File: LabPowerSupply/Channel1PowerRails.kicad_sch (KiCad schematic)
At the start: 8 parts

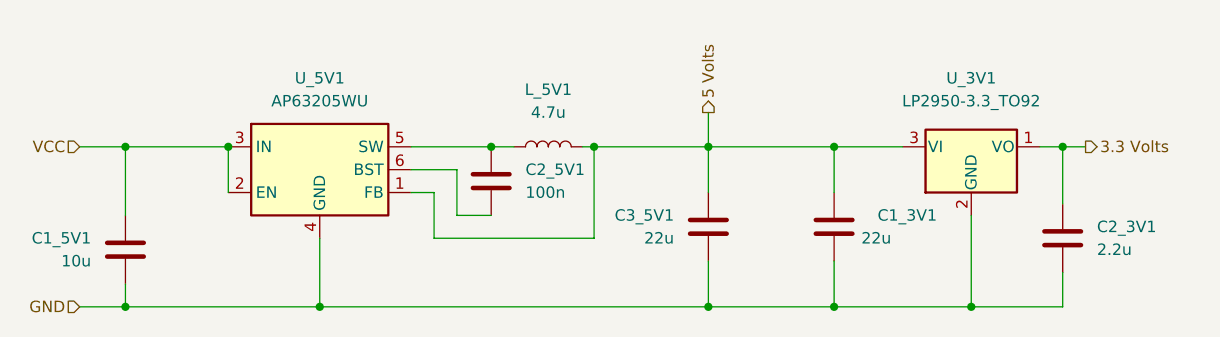
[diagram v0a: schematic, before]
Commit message: Fixed 3.3v footprint
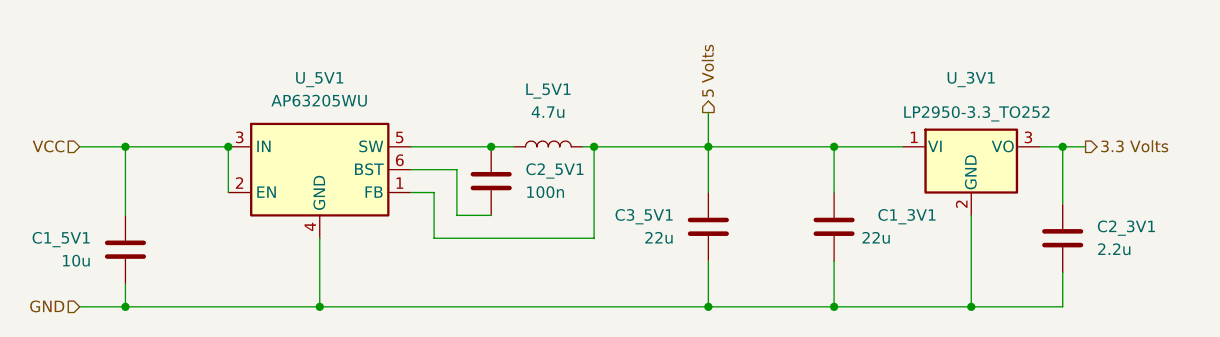
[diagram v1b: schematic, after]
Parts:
- U_3V1: value LP2950-3.3_TO92 -> LP2950-3.3_TO252; footprint Package_TO_SOT_SMD:TO-252-3_TabPin4 -> Package_TO_SOT_SMD:TO-252-2; symbol Regulator_Linear:LP2950-3.3_TO92 -> Regulator_Linear:LP2950-3.3_TO252
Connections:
- net 3.3 Volts: now also U_3V1.3 (VO); no longer U_3V1.1 (VO)
- net 5 Volts: now also U_3V1.1 (VI); no longer U_3V1.3 (VI)
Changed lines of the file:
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@@
     (pin "2")
   )
-  (symbol (lib_id "Regulator_Linear:LP2950-3.3_TO92") (at 196.85 88.9 0) (unit 1)
-    (in_bom yes) (on_board yes) (fields_autoplaced)
+  (symbol (lib_id "Regulator_Linear:LP2950-3.3_TO252") (at 196.85 88.9 0) (unit 1)
+    (in_bom yes) (on_board yes)
     (property "Reference" "U_3V1" (id 0) (at 196.85 81.28 0))
-    (property "Value" "LP2950-3.3_TO92" (id 1) (at 196.85 83.82 0))
-    (property "Footprint" "Package_TO_SOT_SMD:TO-252-3_TabPin4" (id 2) (at 196.85 83.185 0)
+    (property "Value" "LP2950-3.3_TO252" (id 1) (at 189.23 85.09 0)
+      (effects (font (size 1.27 1.27)) (justify left))
+    )
+    (property "Footprint" "Package_TO_SOT_SMD:TO-252-2" (id 2) (at 196.85 83.185 0)
       (effects (font (size 1.27 1.27) italic) hide)
     )

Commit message: Updated Part List
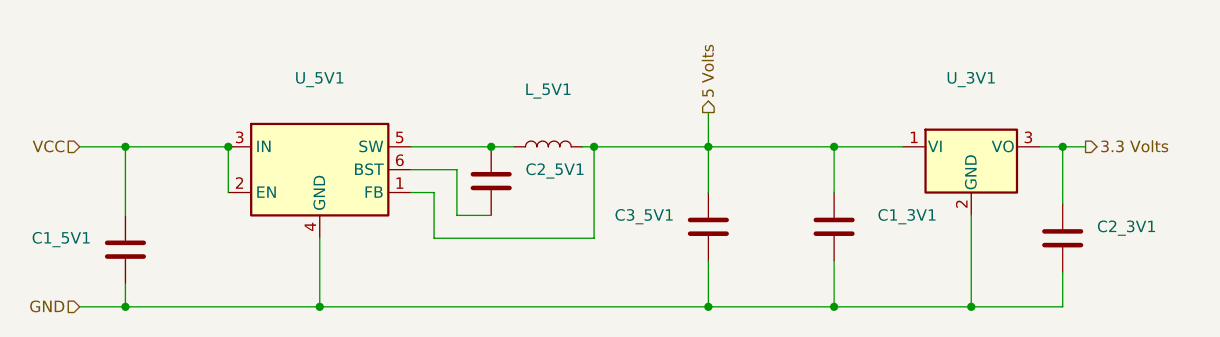
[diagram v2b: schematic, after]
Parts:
- C1_3V1, C3_5V1: value 22u -> (none); footprint Capacitor_SMD:C_1210_3225Metric -> (none)
- C1_5V1: value 10u -> (none); footprint Capacitor_SMD:C_1206_3216Metric -> (none)
- C2_3V1: value 2.2u -> (none); footprint Capacitor_SMD:C_0805_2012Metric -> (none)
- C2_5V1: value 100n -> (none); footprint Capacitor_SMD:C_0603_1608Metric -> (none)
- L_5V1: value 4.7u -> (none); footprint Inductor_SMD:L_Sumida_CDMC6D28_7.25x6.5mm -> (none)
- U_3V1: value LP2950-3.3_TO252 -> (none); footprint Package_TO_SOT_SMD:TO-252-2 -> (none)
- U_5V1: value AP63205WU -> (none); footprint Package_TO_SOT_SMD:TSOT-23-6 -> (none)
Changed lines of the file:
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@@
       (effects (font (size 1.27 1.27)) (justify right))
     )
-    (property "Value" "22u" (id 1) (at 187.96 99.06 0)
+    (property "Value" "" (id 1) (at 187.96 99.06 0)
       (effects (font (size 1.27 1.27)) (justify right))
     )
-    (property "Footprint" "Capacitor_SMD:C_1210_3225Metric" (id 2) (at 182.5752 93.98 0)
+    (property "Footprint" "" (id 2) (at 182.5752 93.98 0)
       (effects (font (size 1.27 1.27)) hide)
     )
@@
       (effects (font (size 1.27 1.27)) (justify left))
     )
-    (property "Value" "2.2u" (id 1) (at 210.82 100.3299 0)
+    (property "Value" "" (id 1) (at 210.82 100.3299 0)
       (effects (font (size 1.27 1.27)) (justify left))
     )
-    (property "Footprint" "Capacitor_SMD:C_0805_2012Metric" (id 2) (at 207.9752 102.87 0)
+    (property "Footprint" "" (id 2) (at 207.9752 102.87 0)
       (effects (font (size 1.27 1.27)) hide)
     )
@@
     (in_bom yes) (on_board yes) (fields_autoplaced)
     (property "Reference" "L_5V1" (id 0) (at 149.86 82.55 90))
-    (property "Value" "4.7u" (id 1) (at 149.86 85.09 90))
-    (property "Footprint" "Inductor_SMD:L_Sumida_CDMC6D28_7.25x6.5mm" (id 2) (at 149.86 88.9 0)
+    (property "Value" "" (id 1) (at 149.86 85.09 90))
+    (property "Footprint" "" (id 2) (at 149.86 88.9 0)
       (effects (font (size 1.27 1.27)) hide)
     )
@@
     (in_bom yes) (on_board yes)
     (property "Reference" "U_3V1" (id 0) (at 196.85 81.28 0))
-    (property "Value" "LP2950-3.3_TO252" (id 1) (at 189.23 85.09 0)
+    (property "Value" "" (id 1) (at 189.23 85.09 0)
       (effects (font (size 1.27 1.27)) (justify left))
     )
-    (property "Footprint" "Package_TO_SOT_SMD:TO-252-2" (id 2) (at 196.85 83.185 0)
+    (property "Footprint" "" (id 2) (at 196.85 83.185 0)
       (effects (font (size 1.27 1.27) italic) hide)
     )
@@
       (effects (font (size 1.27 1.27)) (justify right))
     )
-    (property "Value" "10u" (id 1) (at 99.06 101.5999 0)
+    (property "Value" "" (id 1) (at 99.06 101.5999 0)
       (effects (font (size 1.27 1.27)) (justify right))
     )
-    (property "Footprint" "Capacitor_SMD:C_1206_3216Metric" (id 2) (at 103.8352 96.52 0)
+    (property "Footprint" "" (id 2) (at 103.8352 96.52 0)
       (effects (font (size 1.27 1.27)) hide)
     )
@@
       (effects (font (size 1.27 1.27)) (justify right))
     )
-    (property "Value" "22u" (id 1) (at 163.83 99.0599 0)
+    (property "Value" "" (id 1) (at 163.83 99.0599 0)
       (effects (font (size 1.27 1.27)) (justify right))
     )
-    (property "Footprint" "Capacitor_SMD:C_1210_3225Metric" (id 2) (at 168.6052 93.98 0)
+    (property "Footprint" "" (id 2) (at 168.6052 93.98 0)
       (effects (font (size 1.27 1.27)) hide)
     )
@@
       (effects (font (size 1.27 1.27)) (justify left))
     )
-    (property "Value" "100n" (id 1) (at 147.32 93.9799 0)
+    (property "Value" "" (id 1) (at 147.32 93.9799 0)
       (effects (font (size 1.27 1.27)) (justify left))
     )
-    (property "Footprint" "Capacitor_SMD:C_0603_1608Metric" (id 2) (at 144.4752 96.52 0)
+    (property "Footprint" "" (id 2) (at 144.4752 96.52 0)
       (effects (font (size 1.27 1.27)) hide)
     )
@@
     (in_bom yes) (on_board yes) (fields_autoplaced)
     (property "Reference" "U_5V1" (id 0) (at 124.46 81.28 0))
-    (property "Value" "AP63205WU" (id 1) (at 124.46 83.82 0))
-    (property "Footprint" "Package_TO_SOT_SMD:TSOT-23-6" (id 2) (at 124.46 114.3 0)
+    (property "Value" "" (id 1) (at 124.46 83.82 0))
+    (property "Footprint" "" (id 2) (at 124.46 114.3 0)
       (effects (font (size 1.27 1.27)) hide)
     )
